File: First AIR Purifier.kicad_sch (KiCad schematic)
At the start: 0 parts

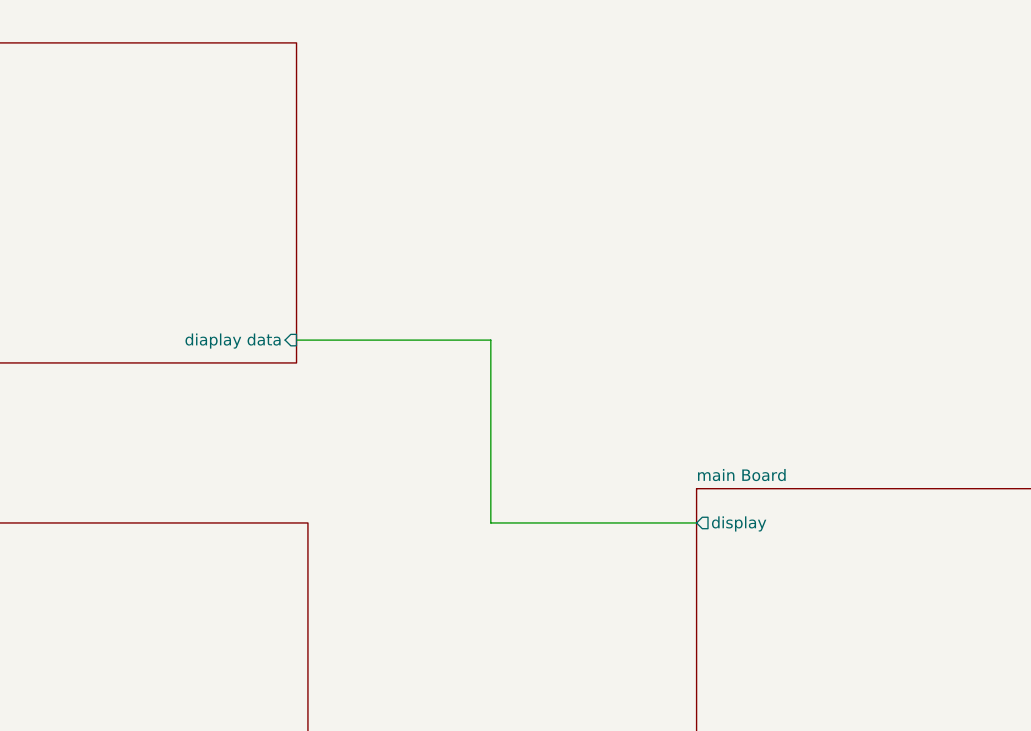
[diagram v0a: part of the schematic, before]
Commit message: added display
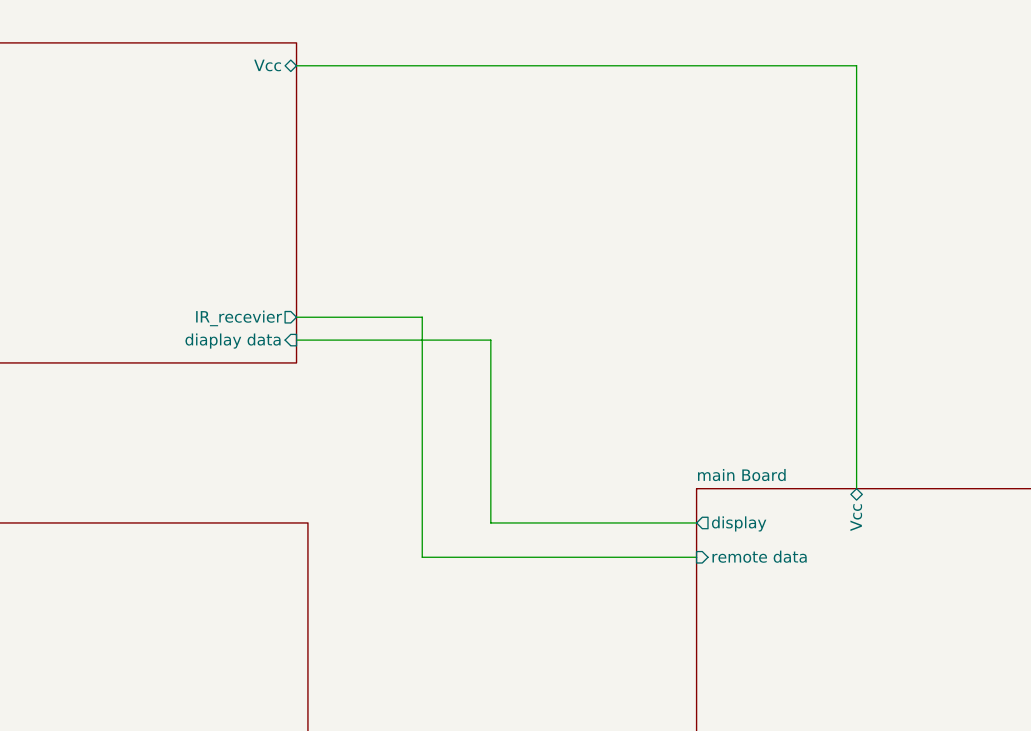
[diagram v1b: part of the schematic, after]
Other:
- sheet Display Unit ports: added IR_recevier, Vcc; removed none
- sheet main Board ports: added Vcc, remote data; removed none
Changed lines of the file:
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@@
+	(wire
+		(pts
+			(xy 91.44 57.15) (xy 105.41 57.15)
+		)
+		(stroke
+			(width 0)
+			(type default)
+		)
+	)
+	(wire
+		(pts
+			(xy 153.67 76.2) (xy 153.67 29.21)
+		)
+		(stroke
+			(width 0)
+			(type default)
+		)
+	)
+	(wire
+		(pts
+			(xy 105.41 57.15) (xy 105.41 83.82)
+		)
+		(stroke
+			(width 0)
+			(type default)
+		)
+	)
 	(wire
 		(pts
@@
 	(wire
 		(pts
+			(xy 153.67 29.21) (xy 91.44 29.21)
+		)
+		(stroke
+			(width 0)
+			(type default)
+		)
+	)
+	(wire
+		(pts
 			(xy 91.44 59.69) (xy 113.03 59.69)
+		)
+		(stroke
+			(width 0)
+			(type default)
+		)
+	)
+	(wire
+		(pts
+			(xy 105.41 83.82) (xy 135.89 83.82)
 		)
 		(stroke
@@
 			)
 		)
+		(pin "Vcc" bidirectional
+			(at 91.44 29.21 0)
+			(effects
+				(font
+					(size 1.27 1.27)
+				)
+				(justify right)
+			)
+		)
+		(pin "IR_recevier" output
+			(at 91.44 57.15 0)
+			(effects
+				(font
+					(size 1.27 1.27)
+				)
+				(justify right)
+			)
+		)
 		(instances
 			(project "First AIR Purifier"
@@
 			(effects
 				(font
+					(size 1.27 1.27)
+				)
+				(justify left)
+			)
+		)
+		(pin "Vcc" bidirectional
+			(at 153.67 76.2 90)
+			(effects
+				(font
+					(size 1.27 1.27)
+				)
+				(justify right)
+			)
+		)
+		(pin "remote data" input
+			(at 135.89 83.82 180)
+			(effects
+				(font
